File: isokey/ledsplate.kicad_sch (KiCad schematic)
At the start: 28 parts, among them SW1 Cherry, SW2 Cherry, SW3 Cherry, SW4 Cherry, SW5 Cherry

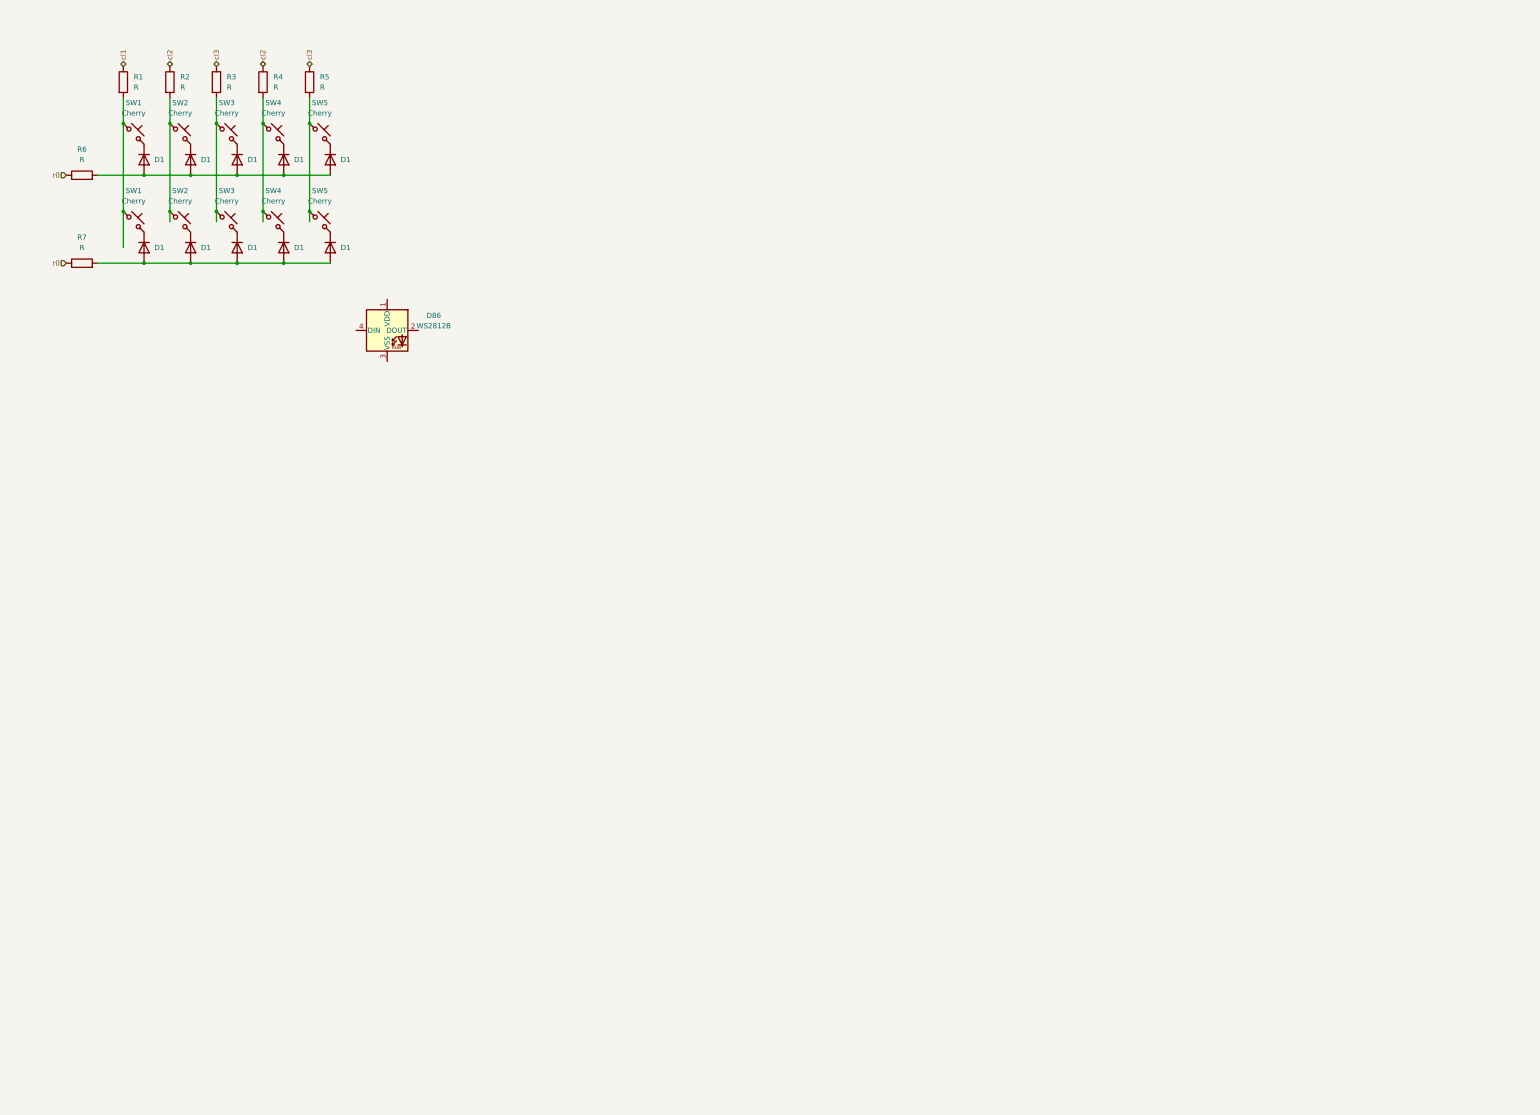
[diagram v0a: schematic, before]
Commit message: Add leds and extra connectors
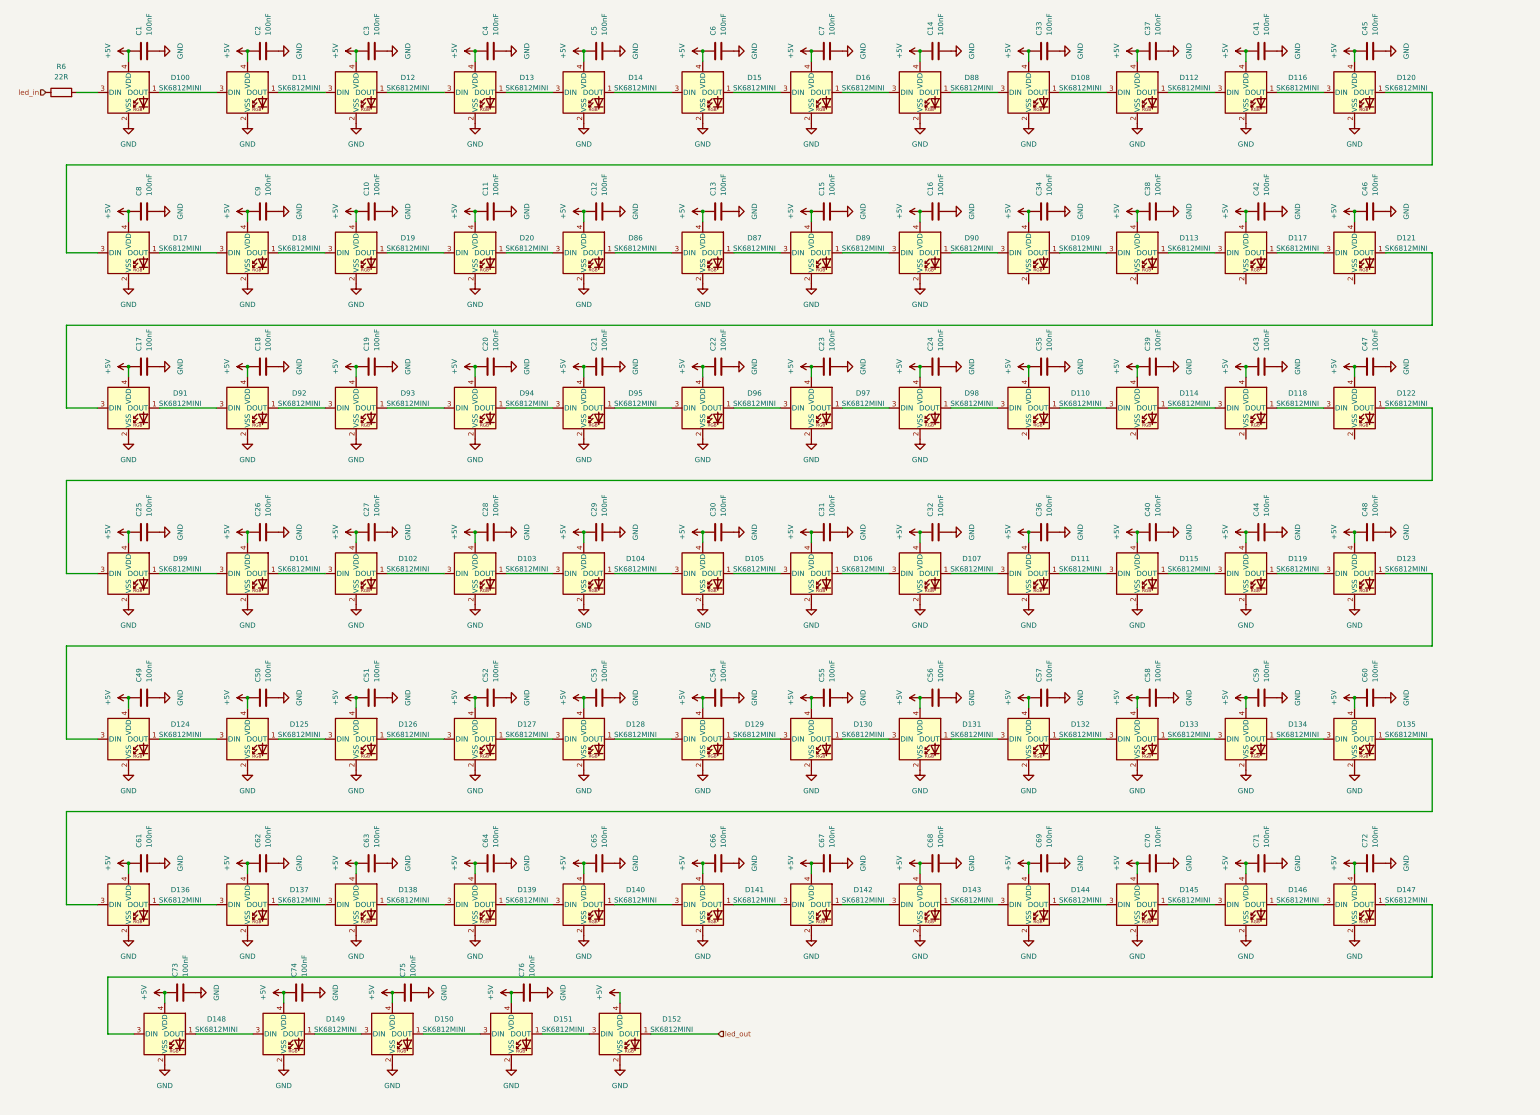
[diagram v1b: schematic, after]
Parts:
- removed D1 (x10): 1N4448W, Diode_SMD:D_SOD-123, symbol Diode:1N4448W
- removed D86: WS2812B, LED_SMD:LED_WS2812B_PLCC4_5.0x5.0mm_P3.2mm, symbol LED:WS2812B
- removed R1, R2, R3, R4, R5, R7: R, symbol Device:R
- removed SW1 (x2), SW2 (x2), SW3 (x2), SW4 (x2), SW5 (x2): Cherry, symbol Switch:SW_Push_45deg
- added C1, C10, C11, C12, C13, C14, C15, C16, C17, C18, C19, C2, C20, C21, C22, C23, C24, C25, C26, C27, C28, C29, C3, C30, C31, C32, C33, C34, C35, C36, C37, C38, C39, C4, C40, C41, C42, C43, C44, C45, C46, C47, C48, C49, C5, C50, C51, C52, C53, C54, C55, C56, C57, C58, C59, C6, C60, C61, C62, C63, C64, C65, C66, C67, C68, C69, C7, C70, C71, C72, C73, C74, C75, C76, C8, C9: 100nF, symbol Device:C
- added D100, D101, D102, D103, D104, D105, D106, D107, D108, D109, D11, D110, D111, D112, D113, D114, D115, D116, D117, D118, D119, D12, D120, D121, D122, D123, D124, D125, D126, D127, D128, D129, D13, D130, D131, D132, D133, D134, D135, D136, D137, D138, D139, D14, D140, D141, D142, D143, D144, D145, D146, D147, D148, D149, D15, D150, D151, D152, D16, D17, D18, D19, D20, D86, D87, D88, D89, D90, D91, D92, D93, D94, D95, D96, D97, D98, D99: SK6812MINI, LED_SMD:LED_SK6812MINI_PLCC4_3.5x3.5mm_P1.75mm, symbol LED:SK6812MINI
- R6: value R -> 22R
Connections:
- net at R6.2: now also D100.3 (DIN)
- net r0 renamed led_in
- new net: D20.1 (DOUT), D86.3 (DIN)
- new net: D19.1 (DOUT), D20.3 (DIN)
- new net: D148.1 (DOUT), D149.3 (DIN)
- new net: D147.1 (DOUT), D148.3 (DIN)
- new net: D108.1 (DOUT), D112.3 (DIN)
- new net: D108.3 (DIN), D88.1 (DOUT)
- new net: D144.1 (DOUT), D145.3 (DIN)
- new net: D143.1 (DOUT), D144.3 (DIN)
- new net: D97.1 (DOUT), D98.3 (DIN)
- new net: D96.1 (DOUT), D97.3 (DIN)
- new net: D120.1 (DOUT), D17.3 (DIN)
- new net: D116.1 (DOUT), D120.3 (DIN)
- new net: D107.1 (DOUT), D111.3 (DIN)
- new net: D106.1 (DOUT), D107.3 (DIN)
- new net: D16.1 (DOUT), D88.3 (DIN)
- new net: D149.1 (DOUT), D150.3 (DIN)
- new net: D146.1 (DOUT), D147.3 (DIN)
- new net: D151.1 (DOUT), D152.3 (DIN)
- new net: D150.1 (DOUT), D151.3 (DIN)
- new net: D93.1 (DOUT), D94.3 (DIN)
- new net: D92.1 (DOUT), D93.3 (DIN)
- new net: D136.1 (DOUT), D137.3 (DIN)
- new net: D135.1 (DOUT), D136.3 (DIN)
- new net: D139.1 (DOUT), D140.3 (DIN)
- new net: D138.1 (DOUT), D139.3 (DIN)
- new net: D101.1 (DOUT), D102.3 (DIN)
- new net: D101.3 (DIN), D99.1 (DOUT)
- new net: D134.1 (DOUT), D135.3 (DIN)
- new net: D133.1 (DOUT), D134.3 (DIN)
- new net: D115.1 (DOUT), D119.3 (DIN)
- new net: D111.1 (DOUT), D115.3 (DIN)
- new net: D95.1 (DOUT), D96.3 (DIN)
- new net: D87.1 (DOUT), D89.3 (DIN)
- new net: D86.1 (DOUT), D87.3 (DIN)
- new net: D91.1 (DOUT), D92.3 (DIN)
- new net: D127.1 (DOUT), D128.3 (DIN)
- new net: D126.1 (DOUT), D127.3 (DIN)
- new net: D121.1 (DOUT), D91.3 (DIN)
- new net: D89.1 (DOUT), D90.3 (DIN)
- new net: D123.1 (DOUT), D124.3 (DIN)
- new net: D119.1 (DOUT), D123.3 (DIN)
- new net: D13.1 (DOUT), D14.3 (DIN)
- new net: D12.1 (DOUT), D13.3 (DIN)
- new net: D109.3 (DIN), D90.1 (DOUT)
- new net: D131.1 (DOUT), D132.3 (DIN)
- new net: D130.1 (DOUT), D131.3 (DIN)
- new net: D14.1 (DOUT), D15.3 (DIN)
- new net: D94.1 (DOUT), D95.3 (DIN)
- new net: D114.1 (DOUT), D118.3 (DIN)
- new net: D110.1 (DOUT), D114.3 (DIN)
- new net: D15.1 (DOUT), D16.3 (DIN)
- new net: D125.1 (DOUT), D126.3 (DIN)
- new net: D137.1 (DOUT), D138.3 (DIN)
- new net: D11.1 (DOUT), D12.3 (DIN)
- new net: D100.1 (DOUT), D11.3 (DIN)
- new net: D142.1 (DOUT), D143.3 (DIN)
- new net: D141.1 (DOUT), D142.3 (DIN)
- new net: D110.3 (DIN), D98.1 (DOUT)
- new net: D117.1 (DOUT), D121.3 (DIN)
- new net: D113.1 (DOUT), D117.3 (DIN)
- new net: D104.1 (DOUT), D105.3 (DIN)
- new net: D103.1 (DOUT), D104.3 (DIN)
- new net: D112.1 (DOUT), D116.3 (DIN)
- new net: D102.1 (DOUT), D103.3 (DIN)
- new net: D140.1 (DOUT), D141.3 (DIN)
- new net: D105.1 (DOUT), D106.3 (DIN)
- new net: D109.1 (DOUT), D113.3 (DIN)
- new net: D128.1 (DOUT), D129.3 (DIN)
- new net: D129.1 (DOUT), D130.3 (DIN)
- new net: D122.1 (DOUT), D99.3 (DIN)
- new net: D118.1 (DOUT), D122.3 (DIN)
- new net: D124.1 (DOUT), D125.3 (DIN)
- new net: D17.1 (DOUT), D18.3 (DIN)
- new net: D18.1 (DOUT), D19.3 (DIN)
- new net: D145.1 (DOUT), D146.3 (DIN)
- new net: D132.1 (DOUT), D133.3 (DIN)
- new net +5V: C1.1, C10.1, C11.1, C12.1, C13.1, C14.1, C15.1, C16.1, C17.1, C18.1, C19.1, C2.1, C20.1, C21.1, C22.1, C23.1, C24.1, C25.1, C26.1, C27.1, C28.1, C29.1, C3.1, C30.1, C31.1, C32.1, C33.1, C34.1, C35.1, C36.1, C37.1, C38.1, C39.1, C4.1, C40.1, C41.1, C42.1, C43.1, C44.1, C45.1, C46.1, C47.1, C48.1, C49.1, C5.1, C50.1, C51.1, C52.1, C53.1, C54.1, C55.1, C56.1, C57.1, C58.1, C59.1, C6.1, C60.1, C61.1, C62.1, C63.1, C64.1, C65.1, C66.1, C67.1, C68.1, C69.1, C7.1, C70.1, C71.1, C72.1, C73.1, C74.1, C75.1, C76.1, C8.1, C9.1, D100.4 (VDD), D101.4 (VDD), D102.4 (VDD), D103.4 (VDD), D104.4 (VDD), D105.4 (VDD), D106.4 (VDD), D107.4 (VDD), D108.4 (VDD), D109.4 (VDD), D11.4 (VDD), D110.4 (VDD), D111.4 (VDD), D112.4 (VDD), D113.4 (VDD), D114.4 (VDD), D115.4 (VDD), D116.4 (VDD), D117.4 (VDD), D118.4 (VDD), D119.4 (VDD), D12.4 (VDD), D120.4 (VDD), D121.4 (VDD), D122.4 (VDD), D123.4 (VDD), D124.4 (VDD), D125.4 (VDD), D126.4 (VDD), D127.4 (VDD), D128.4 (VDD), D129.4 (VDD), D13.4 (VDD), D130.4 (VDD), D131.4 (VDD), D132.4 (VDD), D133.4 (VDD), D134.4 (VDD), D135.4 (VDD), D136.4 (VDD), D137.4 (VDD), D138.4 (VDD), D139.4 (VDD), D14.4 (VDD), D140.4 (VDD), D141.4 (VDD), D142.4 (VDD), D143.4 (VDD), D144.4 (VDD), D145.4 (VDD), D146.4 (VDD), D147.4 (VDD), D148.4 (VDD), D149.4 (VDD), D15.4 (VDD), D150.4 (VDD), D151.4 (VDD), D152.4 (VDD), D16.4 (VDD), D17.4 (VDD), D18.4 (VDD), D19.4 (VDD), D20.4 (VDD), D86.4 (VDD), D87.4 (VDD), D88.4 (VDD), D89.4 (VDD), D90.4 (VDD), D91.4 (VDD), D92.4 (VDD), D93.4 (VDD), D94.4 (VDD), D95.4 (VDD), D96.4 (VDD), D97.4 (VDD), D98.4 (VDD), D99.4 (VDD)
- new net GND: C1.2, C10.2, C11.2, C12.2, C13.2, C14.2, C15.2, C16.2, C17.2, C18.2, C19.2, C2.2, C20.2, C21.2, C22.2, C23.2, C24.2, C25.2, C26.2, C27.2, C28.2, C29.2, C3.2, C30.2, C31.2, C32.2, C33.2, C34.2, C35.2, C36.2, C37.2, C38.2, C39.2, C4.2, C40.2, C41.2, C42.2, C43.2, C44.2, C45.2, C46.2, C47.2, C48.2, C49.2, C5.2, C50.2, C51.2, C52.2, C53.2, C54.2, C55.2, C56.2, C57.2, C58.2, C59.2, C6.2, C60.2, C61.2, C62.2, C63.2, C64.2, C65.2, C66.2, C67.2, C68.2, C69.2, C7.2, C70.2, C71.2, C72.2, C73.2, C74.2, C75.2, C76.2, C8.2, C9.2, D100.2 (VSS), D101.2 (VSS), D102.2 (VSS), D103.2 (VSS), D104.2 (VSS), D105.2 (VSS), D106.2 (VSS), D107.2 (VSS), D108.2 (VSS), D11.2 (VSS), D111.2 (VSS), D112.2 (VSS), D115.2 (VSS), D116.2 (VSS), D119.2 (VSS), D12.2 (VSS), D120.2 (VSS), D123.2 (VSS), D124.2 (VSS), D125.2 (VSS), D126.2 (VSS), D127.2 (VSS), D128.2 (VSS), D129.2 (VSS), D13.2 (VSS), D130.2 (VSS), D131.2 (VSS), D132.2 (VSS), D133.2 (VSS), D134.2 (VSS), D135.2 (VSS), D136.2 (VSS), D137.2 (VSS), D138.2 (VSS), D139.2 (VSS), D14.2 (VSS), D140.2 (VSS), D141.2 (VSS), D142.2 (VSS), D143.2 (VSS), D144.2 (VSS), D145.2 (VSS), D146.2 (VSS), D147.2 (VSS), D148.2 (VSS), D149.2 (VSS), D15.2 (VSS), D150.2 (VSS), D151.2 (VSS), D152.2 (VSS), D16.2 (VSS), D17.2 (VSS), D18.2 (VSS), D19.2 (VSS), D20.2 (VSS), D86.2 (VSS), D87.2 (VSS), D88.2 (VSS), D89.2 (VSS), D90.2 (VSS), D91.2 (VSS), D92.2 (VSS), D93.2 (VSS), D94.2 (VSS), D95.2 (VSS), D96.2 (VSS), D97.2 (VSS), D98.2 (VSS), D99.2 (VSS)
- new net led_out: D152.1 (DOUT)
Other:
- company: (none) -> IsoKey - asterix24@gmail.com
- moved on the sheet: R6

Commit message: Place all sw
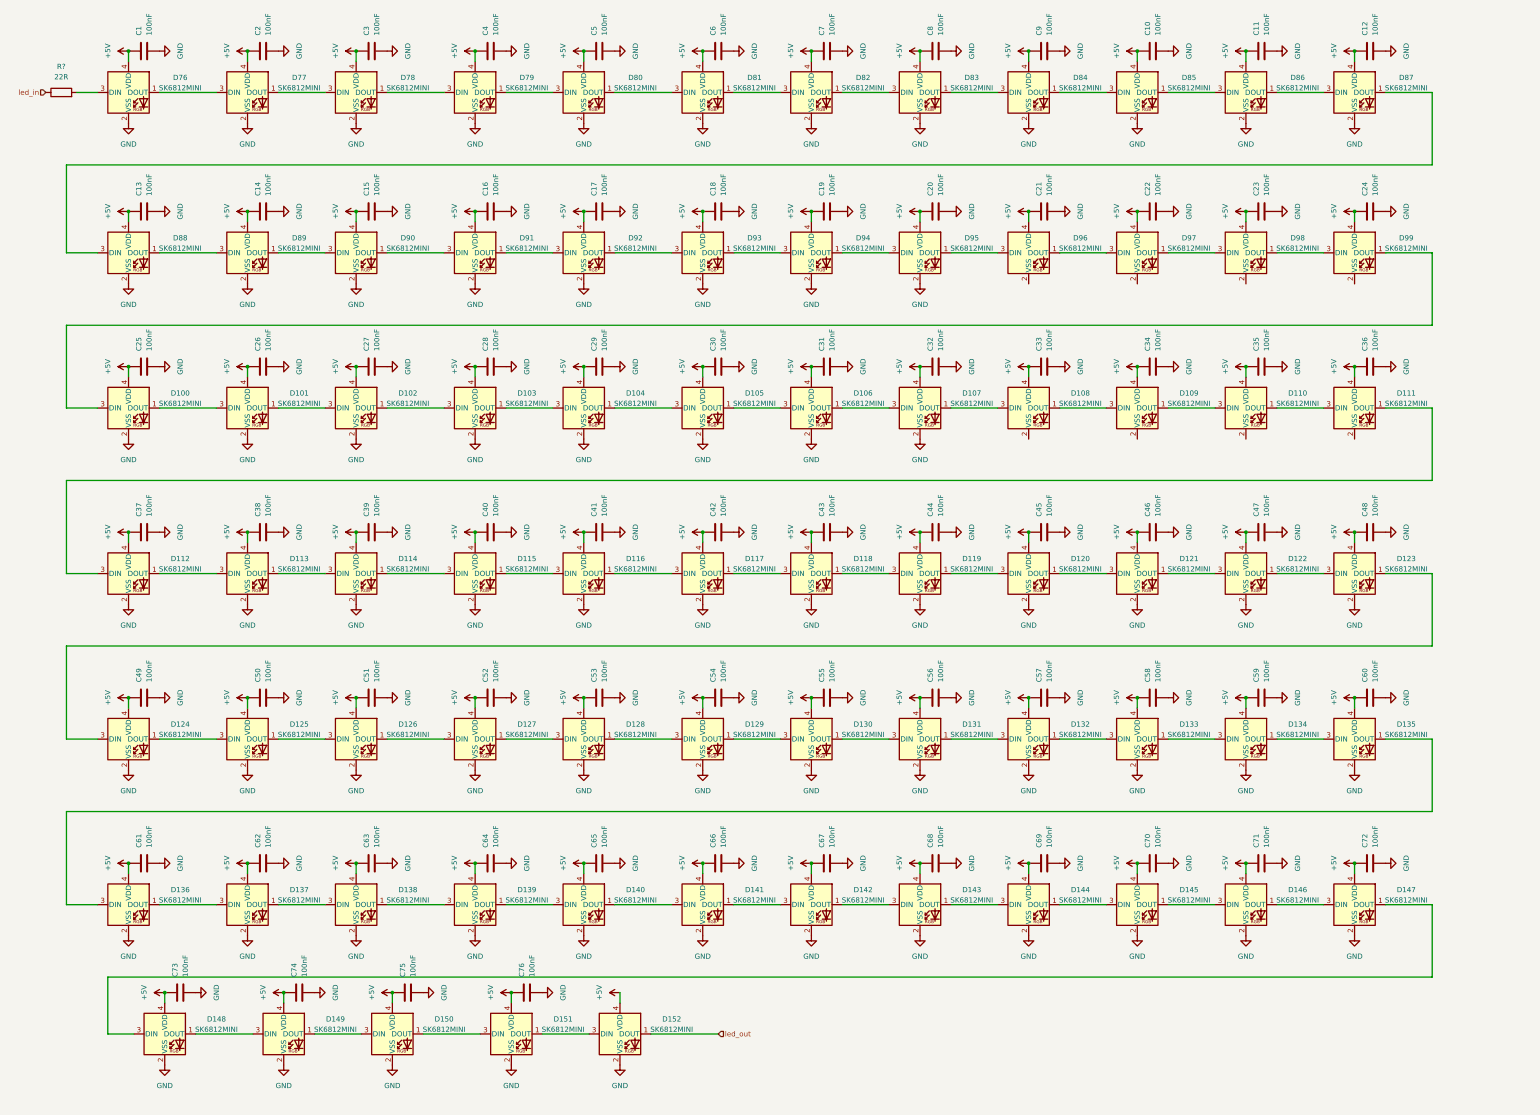
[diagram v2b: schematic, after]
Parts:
- renumbered C37 to C10, C41 to C11, C45 to C12, C8 to C13, C9 to C14, C10 to C15, C11 to C16, C12 to C17, C13 to C18, C15 to C19, C16 to C20, C34 to C21, C38 to C22, C42 to C23, C46 to C24, C17 to C25, C18 to C26, C19 to C27, C20 to C28, C21 to C29, C22 to C30, C23 to C31, C24 to C32, C35 to C33, C39 to C34, C43 to C35, C47 to C36, C25 to C37, C26 to C38, C27 to C39, C28 to C40, C29 to C41, C30 to C42, C31 to C43, C32 to C44, C36 to C45, C40 to C46, C44 to C47, C14 to C8, C33 to C9, D91 to D100, D92 to D101, D93 to D102, D94 to D103, D95 to D104, D96 to D105, D97 to D106, D98 to D107, D110 to D108, D114 to D109, D118 to D110, D122 to D111, D99 to D112, D101 to D113, D102 to D114, D103 to D115, D104 to D116, D105 to D117, D106 to D118, D107 to D119, D111 to D120, D115 to D121, D119 to D122, D100 to D76, D11 to D77, D12 to D78, D13 to D79, D14 to D80, D15 to D81, D16 to D82, D88 to D83, D108 to D84, D112 to D85, D116 to D86, D120 to D87, D17 to D88, D18 to D89, D19 to D90, D20 to D91, D86 to D92, D87 to D93, D89 to D94, D90 to D95, D109 to D96, D113 to D97, D117 to D98, D121 to D99, R6 to R?

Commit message: Place switch and leds
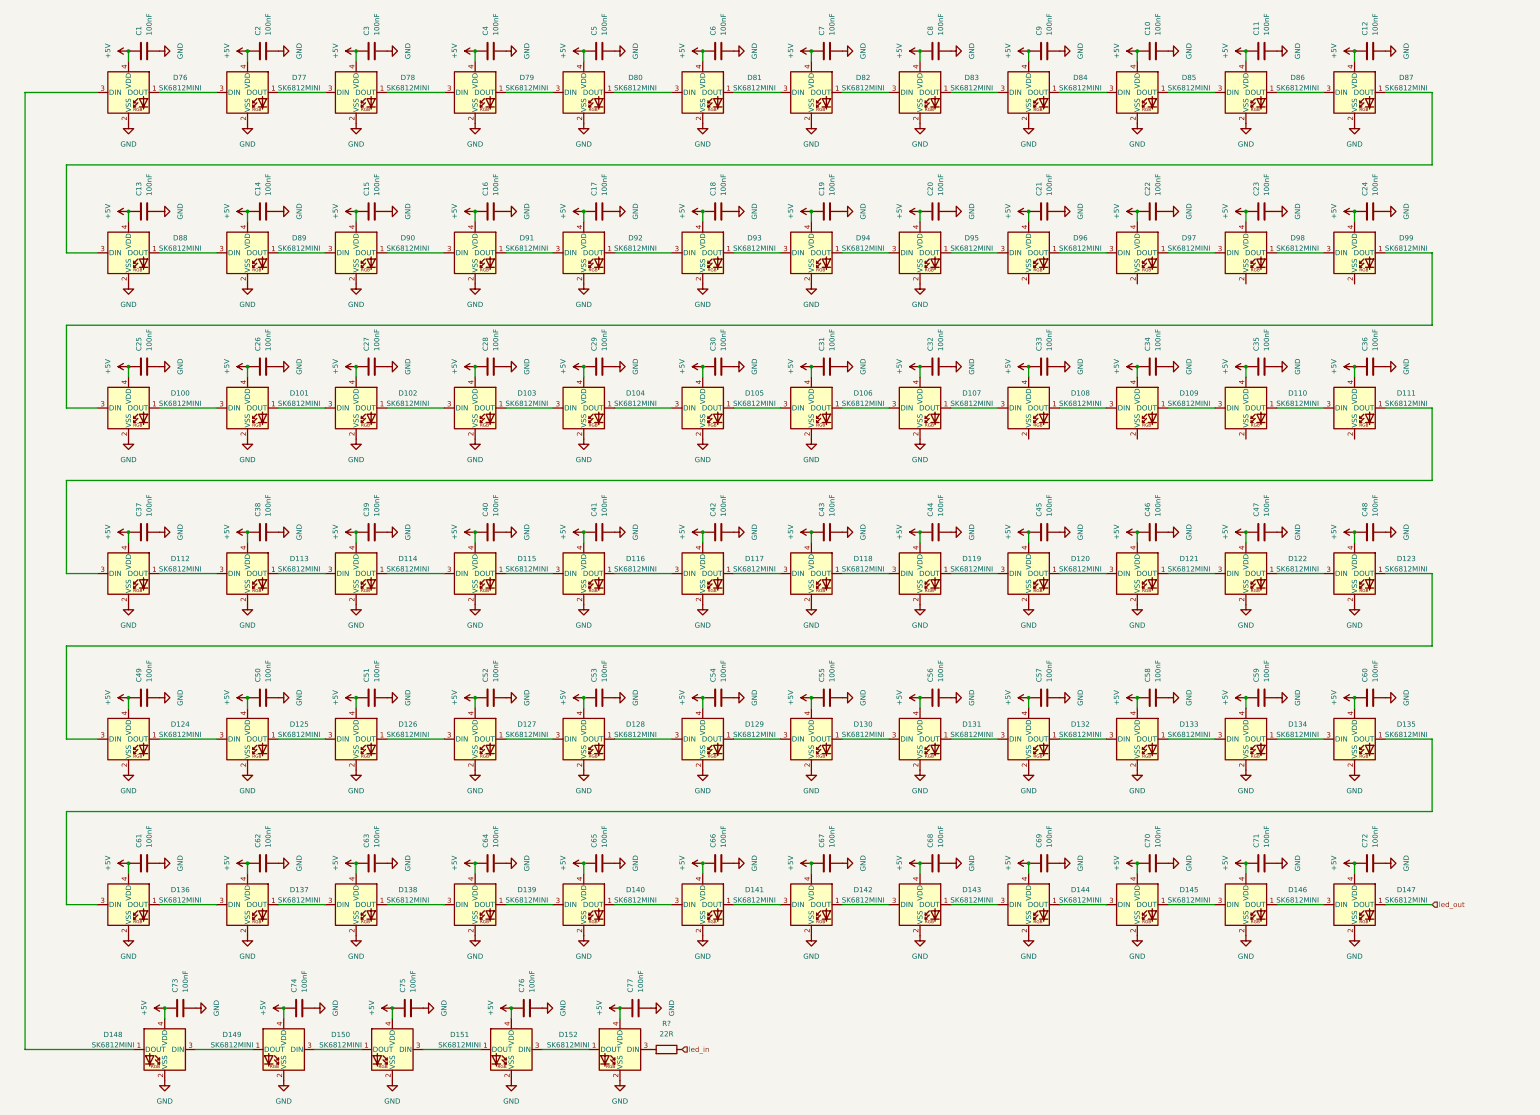
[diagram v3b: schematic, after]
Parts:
- added C77: 100nF, Capacitor_SMD:C_0603_1608Metric_Pad1.08x0.95mm_HandSolder, symbol Device:C
- C1, C10, C11, C12, C13, C14, C15, C16, C17, C18, C19, C2, C20, C21, C22, C23, C24, C25, C26, C27, C28, C29, C3, C30, C31, C32, C33, C34, C35, C36, C37, C38, C39, C4, C40, C41, C42, C43, C44, C45, C46, C47, C48, C49, C5, C50, C51, C52, C53, C54, C55, C56, C57, C58, C59, C6, C60, C61, C62, C63, C64, C65, C66, C67, C68, C69, C7, C70, C71, C72, C73, C74, C75, C76, C8, C9: footprint (none) -> Capacitor_SMD:C_0603_1608Metric_Pad1.08x0.95mm_HandSolder
- R?: footprint (none) -> Resistor_SMD:R_0603_1608Metric_Pad0.98x0.95mm_HandSolder
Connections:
- net +5V: now also C77.1
- net GND: now also C77.2
- net led_out: now also D147.1 (DOUT); no longer D152.1 (DOUT)
- net at D148.1 (DOUT): now also D76.3 (DIN); no longer D149.3 (DIN)
- net at D148.3 (DIN): now also D149.1 (DOUT); no longer D147.1 (DOUT)
- net at D150.3 (DIN): now also D151.1 (DOUT); no longer D149.1 (DOUT)
- net at D152.3 (DIN): now also R?.2; no longer D151.1 (DOUT)
- net at D150.1 (DOUT): now also D149.3 (DIN); no longer D151.3 (DIN)
- new net: D151.3 (DIN), D152.1 (DOUT)
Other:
- moved on the sheet: C73, C74, C75, C76, D148, D149, D150, D151, D152, R?

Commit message: Continue routing
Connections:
- net GND: now also D108.2 (VSS), D109.2 (VSS), D110.2 (VSS), D111.2 (VSS), D96.2 (VSS), D97.2 (VSS), D98.2 (VSS), D99.2 (VSS)
